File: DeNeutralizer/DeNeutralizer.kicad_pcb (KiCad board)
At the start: 2 copper layers, 27.9 x 75.6 mm, 18 parts, among them J1 Screw_Terminal_01x03, J2 Screw_Terminal_01x03, J3 Screw_Terminal_01x03, J4 Screw_Terminal_01x03, J7 Screw_Terminal_01x02, J8 Screw_Terminal_01x05, J9 Screw_Terminal_01x02, U1 PC817

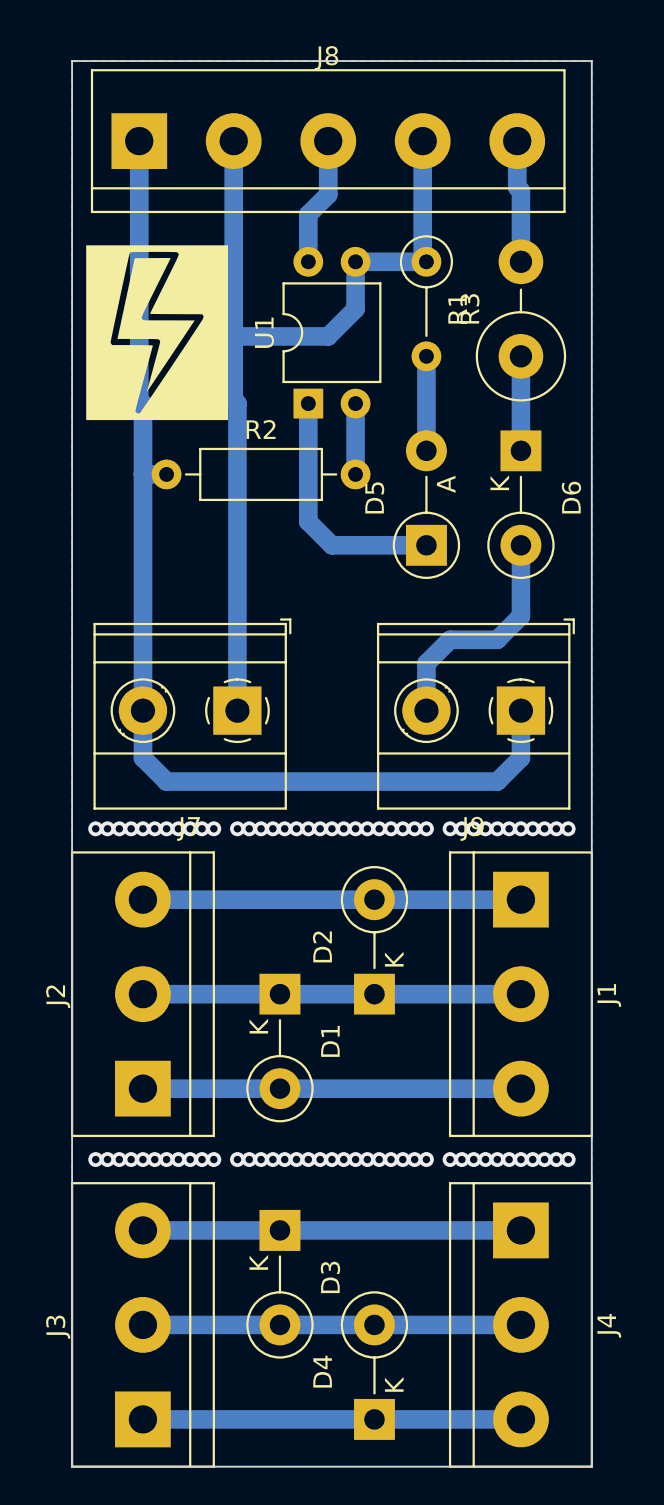
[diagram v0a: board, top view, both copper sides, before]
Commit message: Update PCB contour
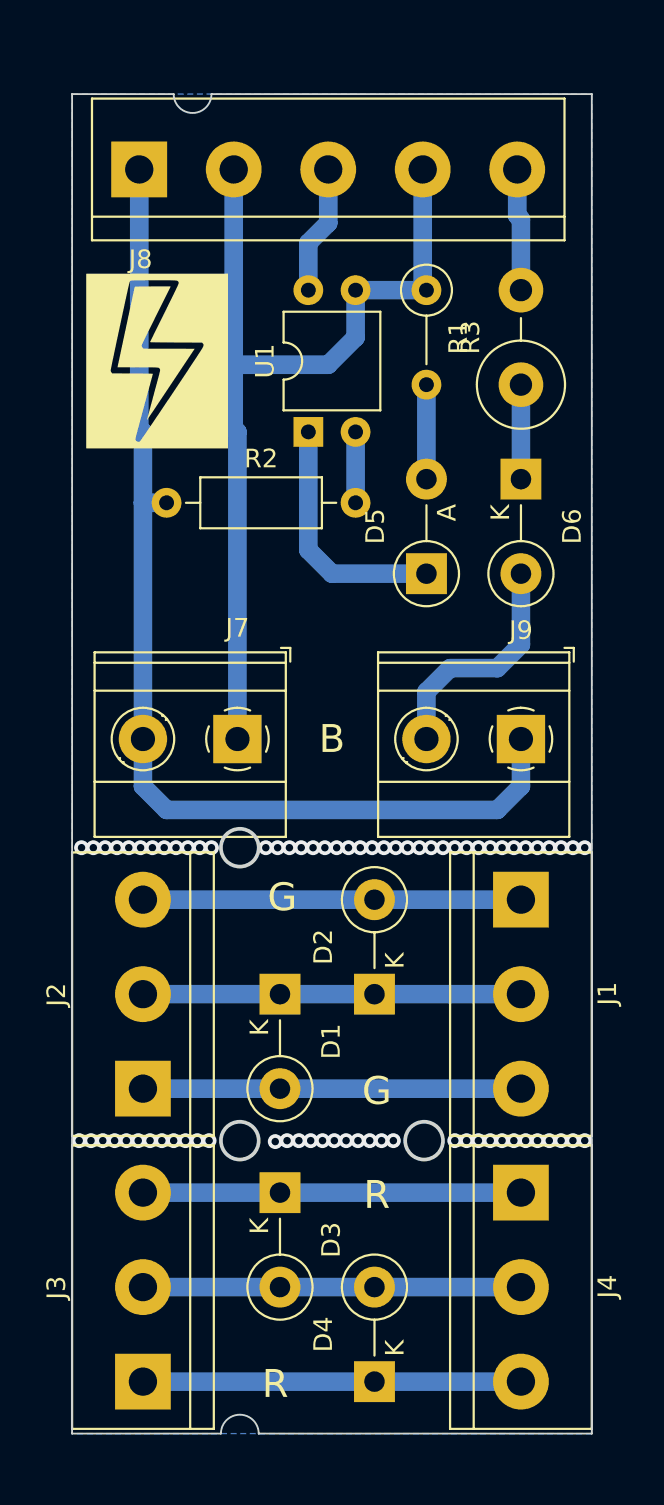
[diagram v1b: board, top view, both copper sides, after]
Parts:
- moved D3 2.03 mm to (128.0, 127.5)
- moved J4 2.03 mm to (141.0, 127.5)
- moved D4 2.03 mm to (133.1, 137.7)
- moved J3 2.03 mm to (120.7, 137.7)
- moved ? 1.52 mm to (121.4, 82.8)
- moved D5 1.52 mm to (135.9, 94.2)
- moved D6 1.52 mm to (141.0, 89.2)
- moved J7 1.52 mm to (125.7, 103.1)
- moved J8 1.52 mm to (120.5, 72.5)
- moved J9 1.52 mm to (141.0, 103.1)
- moved R1 1.52 mm to (141.0, 84.1)
- moved R2 1.52 mm to (121.9, 90.4)
- moved R3 1.52 mm to (135.9, 79.0)
- moved U1 1.52 mm to (129.5, 86.6)
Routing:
- net (no net): vias 78 -> 75
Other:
- board size 27.9 x 75.6 mm -> 27.9 x 72 mm
- board text added: "B"
- board text added: "G"
- board text added: "R"

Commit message: Redesign the PCB
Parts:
- removed ?: LOGO, DeNeutralizer:Lightning
- removed J8: Screw_Terminal_01x05, TerminalBlock:TerminalBlock_bornier-5_P5.08mm
- removed J9: Screw_Terminal_01x02, TerminalBlock_Phoenix:TerminalBlock_Phoenix_MKDS-1,5-2-5.08_1x02_P5.08mm_Horizontal
- added C1: C_Polarized, Capacitor_THT:CP_Radial_D6.3mm_P2.50mm, F.Cu at (138.4, 88.3)
- added C2: C_Polarized, Capacitor_THT:CP_Radial_D8.0mm_P5.00mm, F.Cu at (128.9, 70.5)
- added J5: Screw_Terminal_01x02, TerminalBlock:TerminalBlock_bornier-2_P5.08mm, F.Cu at (134.0, 104.1)
- added J6: Screw_Terminal_01x05, TerminalBlock:TerminalBlock_bornier-5_P5.08mm, F.Cu at (120.7, 98.4)
- J7: footprint TerminalBlock_Phoenix:TerminalBlock_Phoenix_MKDS-1,5-2-5.08_1x02_P5.08mm_Horizontal -> TerminalBlock:TerminalBlock_bornier-2_P5.08mm
- R1: footprint Resistor_THT:R_Axial_DIN0414_L11.9mm_D4.5mm_P5.08mm_Vertical -> Resistor_THT:R_Axial_DIN0207_L6.3mm_D2.5mm_P10.16mm_Horizontal
- R2: footprint Resistor_THT:R_Axial_DIN0207_L6.3mm_D2.5mm_P10.16mm_Horizontal -> Resistor_THT:R_Axial_DIN0207_L6.3mm_D2.5mm_P5.08mm_Vertical
- R3: footprint Resistor_THT:R_Axial_DIN0207_L6.3mm_D2.5mm_P5.08mm_Vertical -> Resistor_THT:R_Axial_DIN0414_L11.9mm_D4.5mm_P5.08mm_Vertical
- moved J7 32.4 mm to (135.9, 72.4), turned to 0 degrees
- moved R1 18.7 mm to (128.9, 98.4), turned to 0 degrees
- moved R2 12.8 mm to (134.0, 94.6), turned to 180 degrees
- moved D6 11.0 mm to (135.9, 79.4), turned to 0 degrees
- moved R3 4.74 mm to (131.4, 80.6), turned to 180 degrees
- moved U1 4.73 mm to (134.0, 88.3), turned to 180 degrees
- moved D5 3.38 mm to (134.0, 91.4), turned to 180 degrees
- moved D2 0.05 mm to (133.1, 116.9)
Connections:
- D6 pad 2: Net-(J9-Pad2) -> Net-(C2-Pad2)
- J7 pad 1: Net-(J8-Pad2) -> Net-(C2-Pad1)
- J7 pad 2: Net-(J7-Pad2) -> Net-(C2-Pad2)
- R1 pad 1: Net-(D6-Pad1) -> Net-(C2-Pad1)
- R1 pad 2: Net-(J8-Pad5) -> Net-(C1-Pad2)
- R2 pad 1: Net-(J7-Pad2) -> Net-(J5-Pad1)
- R2 pad 2: Net-(C1-Pad2) -> Net-(D5-Pad2)
- R3 pad 1: Net-(J8-Pad2) -> Net-(D6-Pad1)
- R3 pad 2: Net-(D5-Pad2) -> Net-(J6-Pad5)
- U1 pad 3: Net-(J8-Pad2) -> Net-(J5-Pad1)
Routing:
- net Net-(C2-Pad1): track 0.00 -> 94.5 mm
- net Net-(J7-Pad2): track 58.4 -> 0.00 mm
- net Net-(J8-Pad2): track 51.1 -> 0.00 mm
- net Net-(J5-Pad1): track 0.00 -> 41.9 mm
- net Net-(C2-Pad2): track 0.00 -> 19.1 mm
- net Net-(C1-Pad2): track 3.81 -> 19.6 mm
- net Net-(J9-Pad2): track 12.5 -> 0.00 mm
- net Net-(J6-Pad5): track 0.00 -> 6.77 mm
- net Net-(J8-Pad5): track 6.57 -> 0.00 mm
- net Net-(C1-Pad1): track 13.2 -> 7.63 mm
- net Net-(D5-Pad2): track 5.08 -> 3.17 mm
- net Net-(J6-Pad3): track 6.93 -> 5.71 mm
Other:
- board text removed: "B"

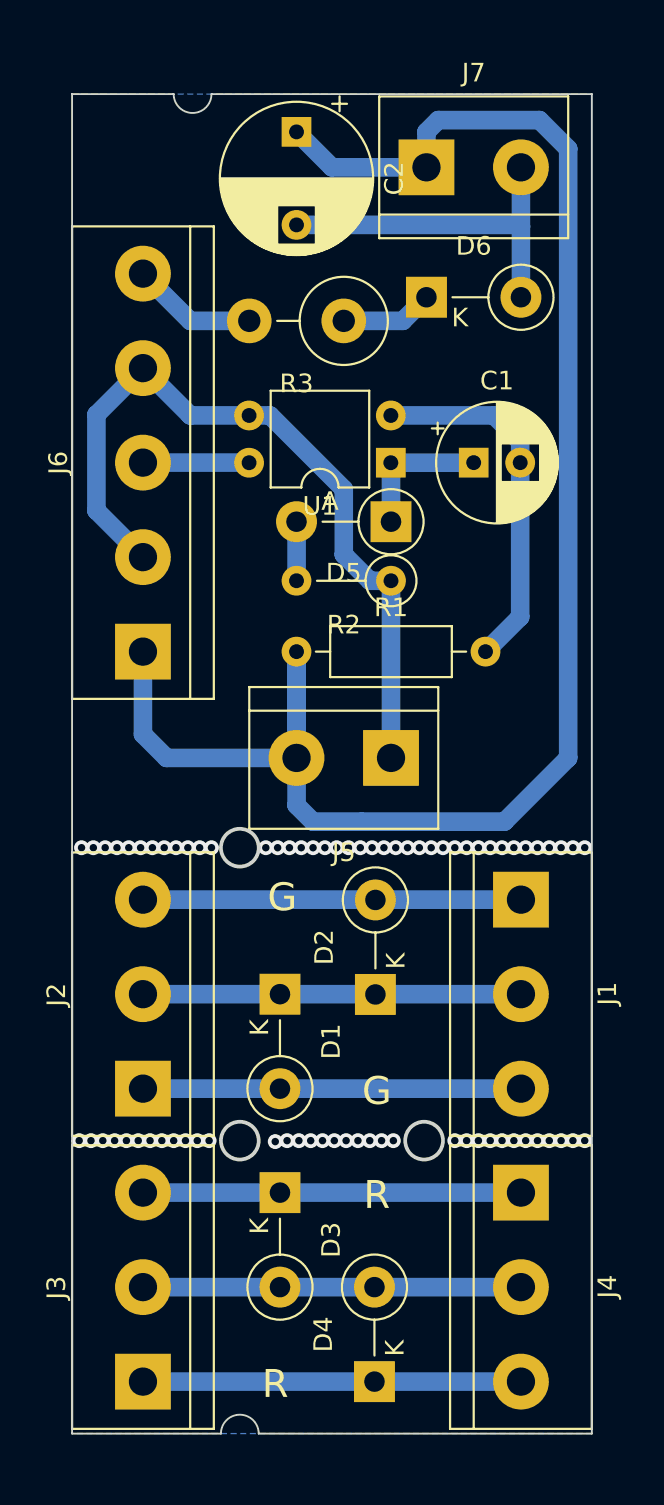
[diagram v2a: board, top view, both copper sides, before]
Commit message: Update components marks locations
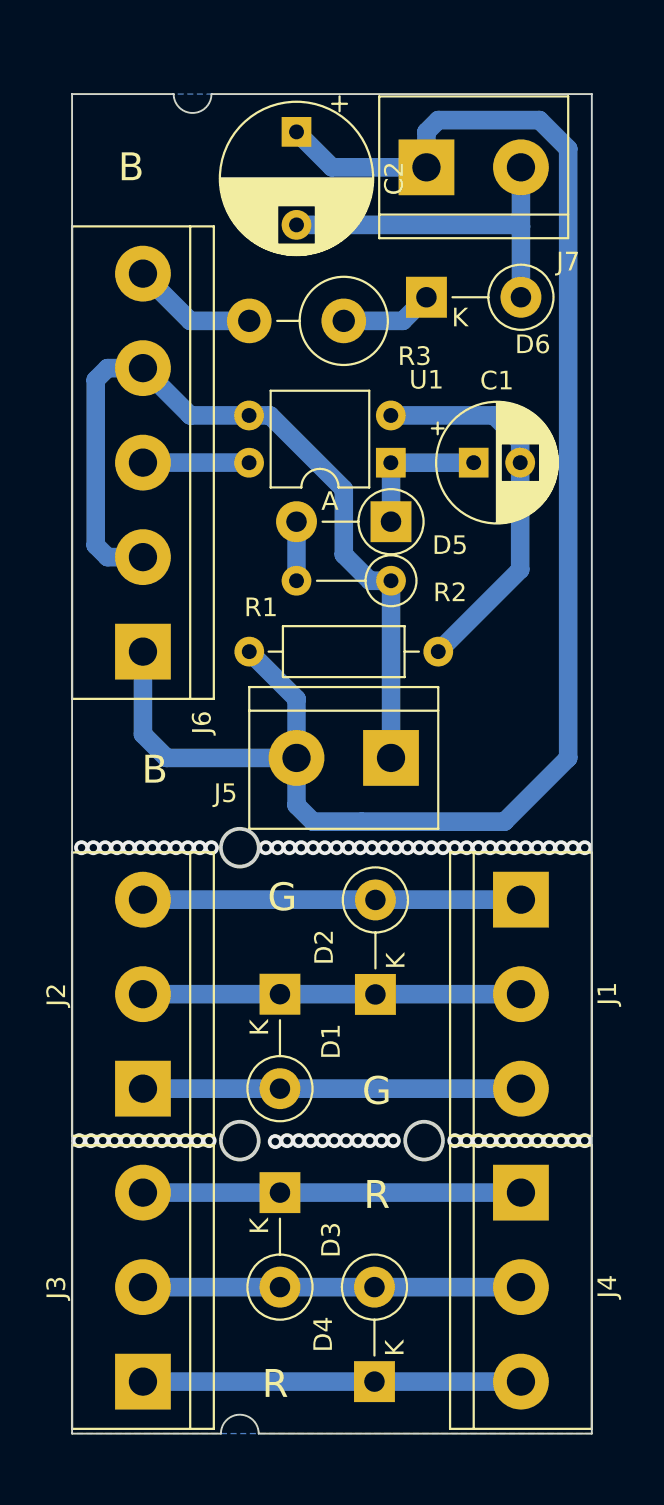
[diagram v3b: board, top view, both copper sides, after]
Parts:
- moved R1 2.54 mm to (126.4, 98.4)
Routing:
- net Net-(C2-Pad1): track 94.5 -> 89.9 mm
- net Net-(J5-Pad1): track 41.9 -> 44.2 mm
- net Net-(C1-Pad2): track 19.6 -> 20.7 mm
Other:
- board text added: "B"
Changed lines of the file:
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@@
     (property "Sheetname" "")
     (attr through_hole)
-    (fp_text reference "J5" (at 2.54 -5.08) (layer "F.SilkS")
+    (fp_text reference "J5" (at 8.89 -1.905) (layer "F.SilkS")
       (effects (font (size 1 1) (thickness 0.15)))
     )
@@
     (property "Sheetname" "")
     (attr through_hole)
-    (fp_text reference "U1" (at 3.81 -2.33) (layer "F.SilkS")
+    (fp_text reference "U1" (at -1.915 4.45) (layer "F.SilkS")
       (effects (font (size 1 1) (thickness 0.15)))
     )
@@
       (effects (font (size 1 1) (thickness 0.15)))
     )
-    (fp_text user "${REFERENCE}" (at 3.81 1.27) (layer "F.Fab")
+    (fp_text user "${REFERENCE}" (at -1.915 4.45) (layer "F.Fab")
       (effects (font (size 1 1) (thickness 0.15)))
     )
@@
     (property "Sheetname" "")
     (attr through_hole)
-    (fp_text reference "R3" (at 2.54 -3.37) (layer "F.SilkS")
+    (fp_text reference "R3" (at -3.81 -1.905) (layer "F.SilkS")
       (effects (font (size 1 1) (thickness 0.15)))
     )
@@
       (effects (font (size 1 1) (thickness 0.15)))
     )
-    (fp_text user "${REFERENCE}" (at 2.54 -3.37) (layer "F.Fab")
+    (fp_text user "${REFERENCE}" (at -3.81 -1.905) (layer "F.Fab")
       (effects (font (size 1 1) (thickness 0.15)))
     )
@@
     (property "Sheetname" "")
     (attr through_hole)
-    (fp_text reference "R2" (at 2.54 -2.37) (layer "F.SilkS")
+    (fp_text reference "R2" (at -3.175 -0.635) (layer "F.SilkS")
       (effects (font (size 1 1) (thickness 0.15)))
     )
@@
       (effects (font (size 1 1) (thickness 0.15)))
     )
-    (fp_text user "${REFERENCE}" (at 2.54 -2.37) (layer "F.Fab")
+    (fp_text user "${REFERENCE}" (at -3.175 -0.635) (layer "F.Fab")
       (effects (font (size 1 1) (thickness 0.15)))
     )
@@
     (property "Sheetname" "")
     (attr through_hole)
-    (fp_text reference "D5" (at 2.54 -2.750635) (layer "F.SilkS")
+    (fp_text reference "D5" (at -3.175 -1.27) (layer "F.SilkS")
       (effects (font (size 1 1) (thickness 0.15)))
     )
@@
       (effects (font (size 1 1) (thickness 0.15)))
     )
-    (fp_text user "${REFERENCE}" (at 2.54 -2.750635) (layer "F.Fab")
+    (fp_text user "${REFERENCE}" (at -3.175 -1.27) (layer "F.Fab")
       (effects (font (size 1 1) (thickness 0.15)))
     )
@@
     (property "Sheetname" "")
     (attr through_hole)
-    (fp_text reference "J7" (at 2.54 -5.08) (layer "F.SilkS")
+    (fp_text reference "J7" (at 7.62 5.08) (layer "F.SilkS")
       (effects (font (size 1 1) (thickness 0.15)))
     )
@@
       (effects (font (size 1 1) (thickness 0.15)))
     )
-    (fp_text user "${REFERENCE}" (at 2.54 0) (layer "F.Fab")
+    (fp_text user "${REFERENCE}" (at -3.81 -3.175) (layer "F.Fab")
       (effects (font (size 1 1) (thickness 0.15)))
     )
@@
     (property "Sheetname" "")
     (attr through_hole)
-    (fp_text reference "D6" (at 2.54 -2.750635) (layer "F.SilkS")
+    (fp_text reference "D6" (at 5.715 2.54) (layer "F.SilkS")
       (effects (font (size 1 1) (thickness 0.15)))
     )
@@
       (effects (font (size 1 1) (thickness 0.15)))
     )
-    (fp_text user "${REFERENCE}" (at 2.54 -2.750635) (layer "F.Fab")
+    (fp_text user "${REFERENCE}" (at 5.715 2.54) (layer "F.Fab")
       (effects (font (size 1 1) (thickness 0.15)))
     )
@@
     (property "Sheetname" "")
     (attr through_hole)
-    (fp_text reference "J6" (at 10.15 -4.55 90) (layer "F.SilkS")
+    (fp_text reference "J6" (at -3.81 3.175 90) (layer "F.SilkS")
       (effects (font (size 1 1) (thickness 0.15)))
     )
@@
   )
   (footprint "Resistor_THT:R_Axial_DIN0207_L6.3mm_D2.5mm_P10.16mm_Horizontal" (layer "F.Cu")
-    (at 128.905 98.425)
+    (at 126.365 98.425)
     (descr "Resistor, Axial_DIN0207 series, Axial, Horizontal, pin pitch=10.16mm, 0.25W = 1/4W, length*diameter=6.3*2.5mm^2, http://cdn-reichelt.de/documents/datenblatt/B400/1_4W%23YAG.pdf")
     (tags "Resistor Axial_DIN0207 series Axial Horizontal pin pitch 10.16mm 0.25W = 1/4W length 6.3mm diameter 2.5mm")
@@
     (property "Sheetname" "")
     (attr through_hole)
-    (fp_text reference "R1" (at 5.08 -2.37) (layer "F.SilkS")
+    (fp_text reference "R1" (at 0.635 -2.37) (layer "F.SilkS")
       (effects (font (size 1 1) (thickness 0.15)))
     )
@@
       (effects (font (size 1 1) (thickness 0.15)))
     )
-    (fp_text user "${REFERENCE}" (at 5.08 0) (layer "F.Fab")
+    (fp_text user "${REFERENCE}" (at 0.635 -1.905) (layer "F.Fab")
       (effects (font (size 1 1) (thickness 0.15)))
     )
@@
   )
   (gr_text "G" (at 133.223 122.047) (layer "F.SilkS")
+    (effects (font (size 1.5 1.5) (thickness 0.3)))
+  )
+  (gr_text "B" (at 121.285 104.775) (layer "F.SilkS")
+    (effects (font (size 1.5 1.5) (thickness 0.3)))
+  )
+  (gr_text "B" (at 120.015 72.39) (layer "F.SilkS")
     (effects (font (size 1.5 1.5) (thickness 0.3)))
   )
@@
   (segment (start 134.62 80.645) (end 135.89 79.375) (width 1) (layer "B.Cu") (net 9))
   (segment (start 131.445 80.645) (end 134.62 80.645) (width 1) (layer "B.Cu") (net 9))
-  (segment (start 140.93 96.56) (end 139.065 98.425) (width 1) (layer "B.Cu") (net 10))
   (segment (start 140.93 87.13363) (end 139.52637 85.73) (width 1) (layer "B.Cu") (net 10))
+  (segment (start 140.93 88.265) (end 140.93 94.02) (width 1) (layer "B.Cu") (net 10))
+  (segment (start 140.93 94.02) (end 136.525 98.425) (width 1) (layer "B.Cu") (net 10))
   (segment (start 140.93 88.265) (end 140.93 87.13363) (width 1) (layer "B.Cu") (net 10))
   (segment (start 139.52637 85.73) (end 133.975 85.73) (width 1) (layer "B.Cu") (net 10))
-  (segment (start 140.93 88.265) (end 140.93 96.56) (width 1) (layer "B.Cu") (net 10))
   (segment (start 140.084 107.566) (end 132.411 107.566) (width 1) (layer "B.Cu") (net 11))
   (segment (start 121.92 104.14) (end 120.65 102.87) (width 1) (layer "B.Cu") (net 11))
+  (segment (start 128.905 104.14) (end 128.905 100.965) (width 1) (layer "B.Cu") (net 11))
   (segment (start 141.965534 69.85) (end 143.51 71.394466) (width 1) (layer "B.Cu") (net 11))
   (segment (start 135.89 72.39) (end 130.81 72.39) (width 1) (layer "B.Cu") (net 11))
+  (segment (start 128.905 100.965) (end 126.365 98.425) (width 1) (layer "B.Cu") (net 11))
   (segment (start 143.51 104.14) (end 140.084 107.566) (width 1) (layer "B.Cu") (net 11))
   (segment (start 128.905 106.68) (end 129.791 107.566) (width 1) (layer "B.Cu") (net 11))
   (segment (start 136.525 69.85) (end 141.965534 69.85) (width 1) (layer "B.Cu") (net 11))
   (segment (start 143.51 71.394466) (end 143.51 104.14) (width 1) (layer "B.Cu") (net 11))
-  (segment (start 128.905 104.14) (end 128.905 98.425) (width 1) (layer "B.Cu") (net 11))
   (segment (start 120.65 102.87) (end 120.65 98.425) (width 1) (layer "B.Cu") (net 11))
   (segment (start 128.905 104.14) (end 121.92 104.14) (width 1) (layer "B.Cu") (net 11))
   (segment (start 135.89 72.39) (end 135.89 70.485) (width 1) (layer "B.Cu") (net 11))
   (segment (start 135.89 70.485) (end 136.525 69.85) (width 1) (layer "B.Cu") (net 11))
-  (segment (start 128.905 104.06) (end 128.905 98.425) (width 1) (layer "B.Cu") (net 11))
   (segment (start 130.81 72.39) (end 128.905 70.485) (width 1) (layer "B.Cu") (net 11))
   (segment (start 128.905 104.14) (end 128.905 106.68) (width 1) (layer "B.Cu") (net 11))
@@
   (segment (start 128.905 75.485) (end 140.89 75.485) (width 1) (layer "B.Cu") (net 12))
   (segment (start 140.89 75.485) (end 140.97 75.565) (width 1) (layer "B.Cu") (net 12))
+  (segment (start 118.11 83.82) (end 118.745 83.185) (width 1) (layer "B.Cu") (net 13))
   (segment (start 126.355 85.73) (end 123.195 85.73) (width 1) (layer "B.Cu") (net 13))
   (segment (start 126.355 85.73) (end 127.48637 85.73) (width 1) (layer "B.Cu") (net 13))
   (segment (start 127.48637 85.73) (end 131.445 89.68863) (width 1) (layer "B.Cu") (net 13))
+  (segment (start 118.745 93.345) (end 118.11 92.71) (width 1) (layer "B.Cu") (net 13))
   (segment (start 133.985 94.615) (end 133.985 104.14) (width 1) (layer "B.Cu") (net 13))
+  (segment (start 118.11 92.71) (end 118.11 83.82) (width 1) (layer "B.Cu") (net 13))
   (segment (start 131.445 93.20637) (end 131.445 89.68863) (width 1) (layer "B.Cu") (net 13))
   (segment (start 133.985 94.615) (end 132.85363 94.615) (width 1) (layer "B.Cu") (net 13))
-  (segment (start 118.15 90.845) (end 120.65 93.345) (width 1) (layer "B.Cu") (net 13))
-  (segment (start 120.65 83.185) (end 118.15 85.685) (width 1) (layer "B.Cu") (net 13))
-  (segment (start 118.15 85.685) (end 118.15 90.845) (width 1) (layer "B.Cu") (net 13))
+  (segment (start 120.65 93.345) (end 118.745 93.345) (width 1) (layer "B.Cu") (net 13))
+  (segment (start 120.65 83.185) (end 118.745 83.185) (width 1) (layer "B.Cu") (net 13))
   (segment (start 123.195 85.73) (end 120.65 83.185) (width 1) (layer "B.Cu") (net 13))
   (segment (start 132.85363 94.615) (end 131.445 93.20637) (width 1) (layer "B.Cu") (net 13))

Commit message: Add safety openings
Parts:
- added R4: 1M/0.6W, Resistor_THT:R_Axial_DIN0414_L11.9mm_D4.5mm_P5.08mm_Vertical, F.Cu at (120.7, 72.4)
- C1: value C_Polarized -> 470uF/10V
- R1, R2: value R -> 57k
- R3: value R -> 10/0.6W
- moved J6 4.45 mm to (120.7, 102.9)
- moved D6 1.27 mm to (135.9, 80.6)
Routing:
- net Net-(C2-Pad2): track 19.1 -> 29.8 mm
- net Net-(C2-Pad1): track 89.9 -> 94.8 mm
- net Net-(J6-Pad3): track 5.71 -> 8.67 mm
- net Net-(J5-Pad1): track 44.2 -> 45.2 mm
- net Net-(D6-Pad1): track 4.97 -> 4.44 mm
- removed copper zone on B.Cu, net (none)
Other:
- outline, holes or cut-outs redrawn
